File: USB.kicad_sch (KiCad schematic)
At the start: 4 parts, among them P1 USB_C_Plug, U7 FE1.1s

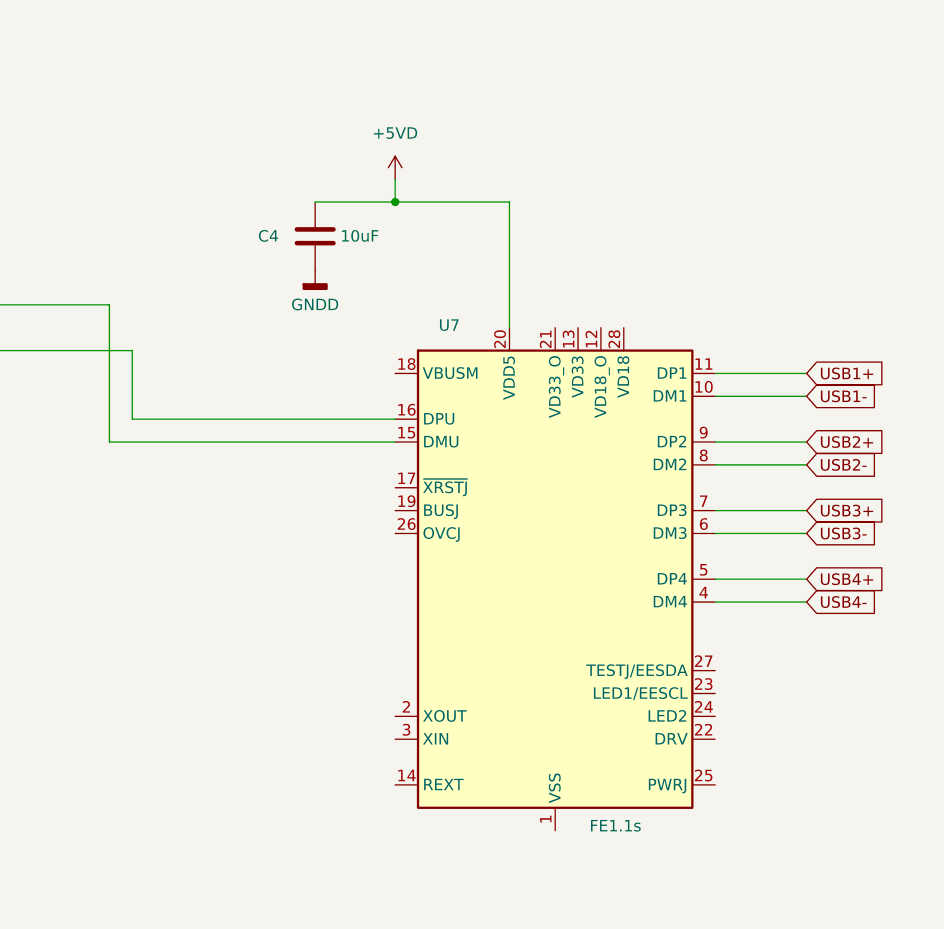
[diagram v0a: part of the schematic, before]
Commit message: Assign footprints to devices
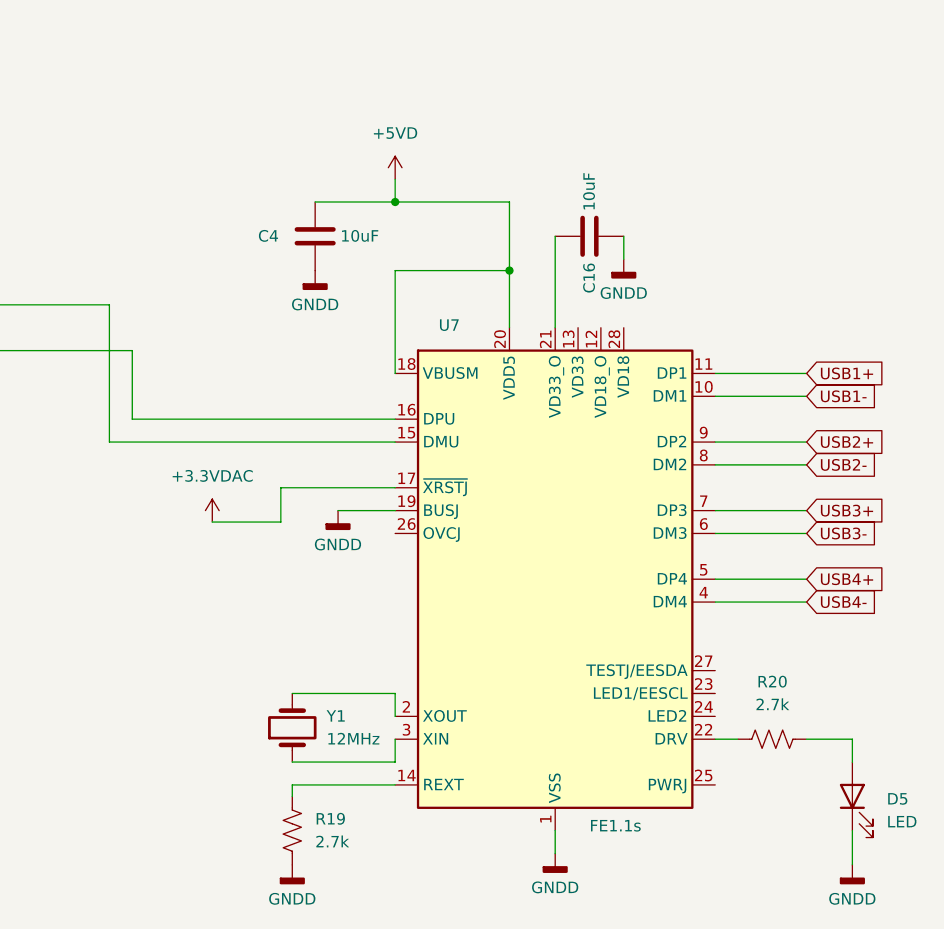
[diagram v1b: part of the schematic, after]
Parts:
- added C16: 10uF, Capacitor_SMD:C_0201_0603Metric, symbol Device:C
- added D5: LED, LED_SMD:LED_0201_0603Metric, symbol Device:LED
- added R19, R20: 2.7k, Resistor_SMD:R_0201_0603Metric, symbol Device:R_US
- added Y1: 12MHz, Crystal:Crystal_SMD_FOX_FE-2Pin_7.5x5.0mm_HandSoldering, symbol Device:Crystal
- C4: footprint (none) -> Capacitor_SMD:C_0201_0603Metric
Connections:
- net +5VD: now also U7.18 (VBUSM)
- net GNDD: now also U7.1 (VSS), U7.19 (BUSJ), C16.2, D5.1 (K), R19.2
- net at U7.14 (REXT): now also R19.1
- net +3.3VDAC: now reaches U7.17 (~{XRSTJ})
- net at U7.2 (XOUT): now also Y1.2
- net at U7.21 (VD33_O): now also C16.1
- net at U7.22 (DRV): now also R20.1
- net at U7.3 (XIN): now also Y1.1
- new net: D5.2 (A), R20.2

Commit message: Place Audio tranformers and cleanup routing.    Re-annotate based on geographical layout.
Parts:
- L1: footprint (none) -> Inductor_SMD:L_CommonModeChoke_Coilcraft_0805USB
- P1: footprint (none) -> Connector_USB:USB_C_Receptacle_GCT_USB4085
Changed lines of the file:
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@@
 			)
 		)
-		(property "Footprint" ""
+		(property "Footprint" "Inductor_SMD:L_CommonModeChoke_Coilcraft_0805USB"
 			(at 55.88 64.77 0)
 			(effects
@@
 			)
 		)
-		(property "Footprint" ""
+		(property "Footprint" "Connector_USB:USB_C_Receptacle_GCT_USB4085"
 			(at 44.45 99.06 0)
 			(effects

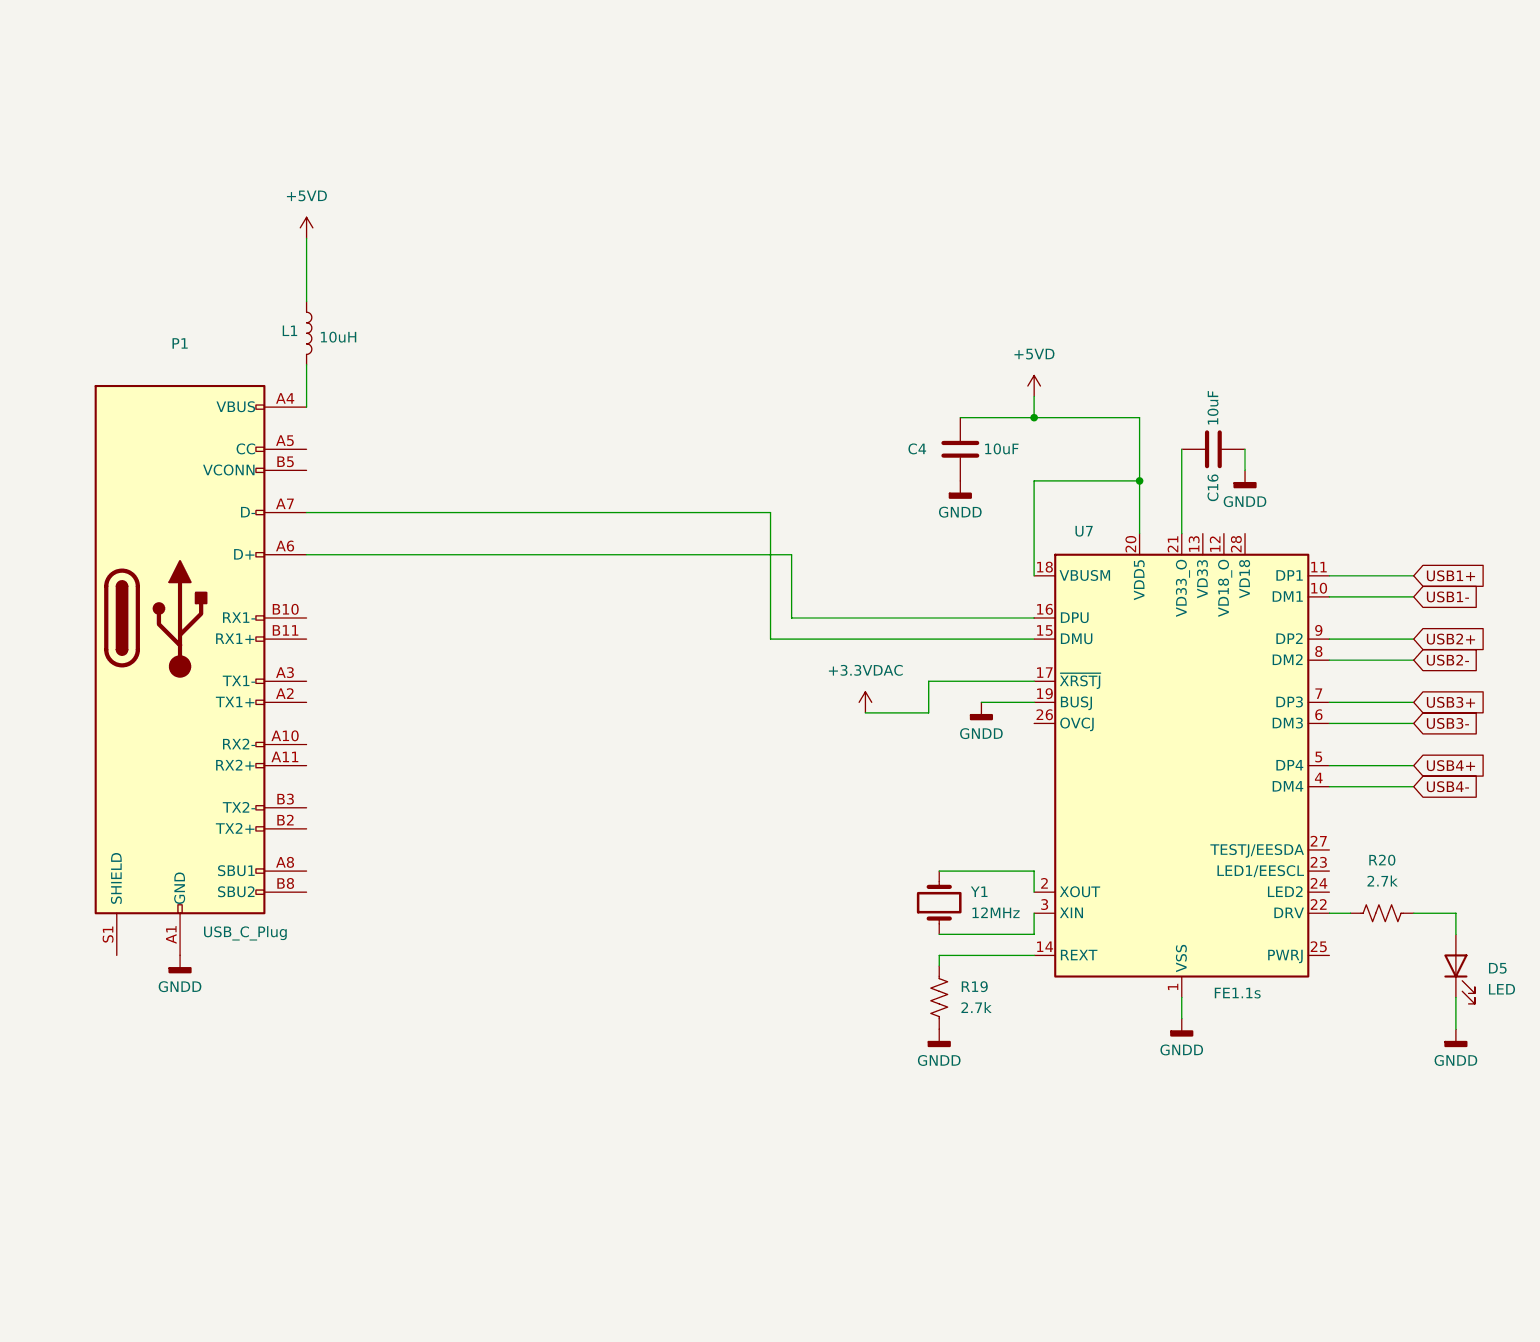
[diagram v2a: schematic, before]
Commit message: Move Radio interface onto it's own sheet, Add mounting holes and case outline
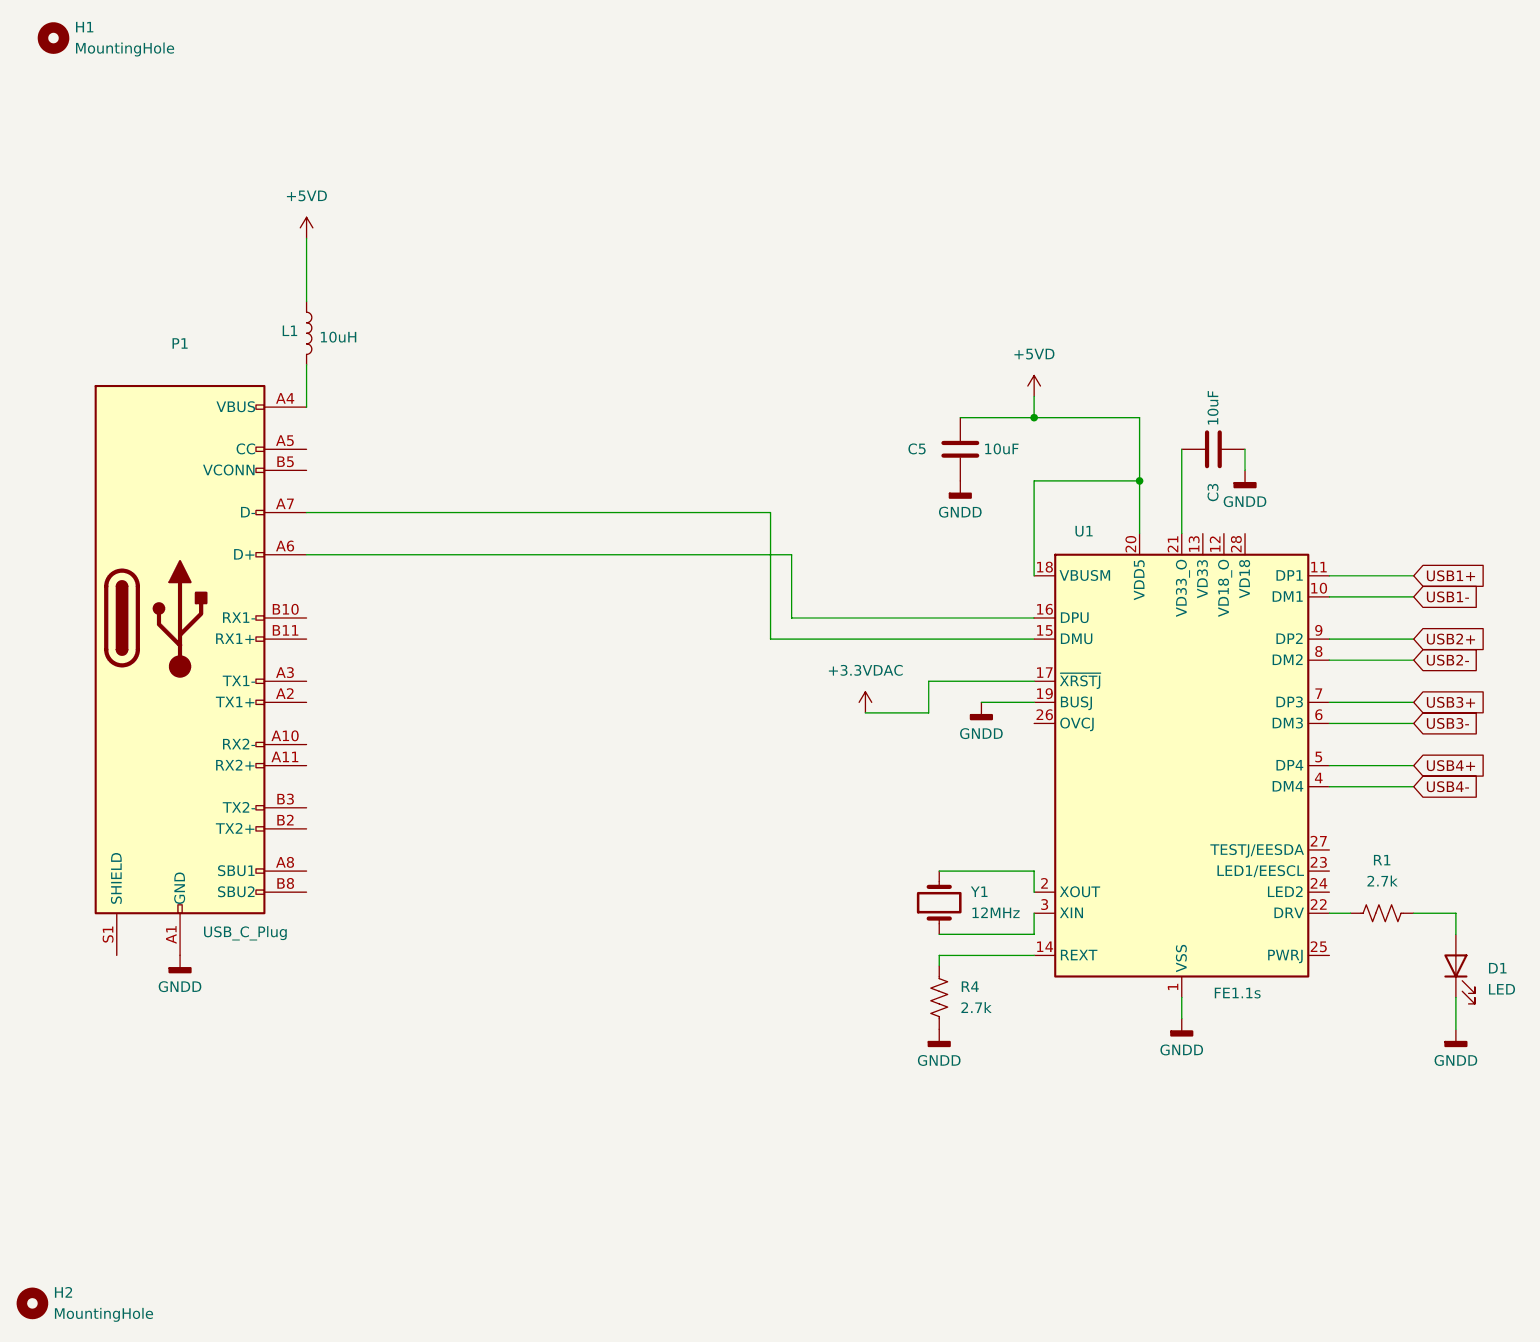
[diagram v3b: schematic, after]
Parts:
- added H1, H2: MountingHole, MountingHole:MountingHole_3.2mm_M3, symbol Mechanical:MountingHole
- renumbered C16 to C3, C4 to C5, D5 to D1, R20 to R1, R19 to R4, U7 to U1
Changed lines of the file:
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@@
 		(dnp no)
 		(fields_autoplaced yes)
-		(property "Reference" "D5"
+		(property "Reference" "D1"
 			(at 198.12 141.2874 90)
 			(effects
@@
 			(project "digital-mode-radio-interface"
 				(path "/a0d4bcf6-6cac-4e92-853e-9083f008b231/09c555a5-1bba-40e9-8ff5-2458ce056329"
-					(reference "D5")
+					(reference "D1")
+					(unit 1)
+				)
+			)
+		)
+	)
+	(symbol
+		(lib_id "Mechanical:MountingHole")
+		(at 22.86 181.61 0)
+		(unit 1)
+		(exclude_from_sim yes)
+		(in_bom no)
+		(on_board yes)
+		(dnp no)
+		(fields_autoplaced yes)
+		(property "Reference" "H2"
+			(at 25.4 180.3399 0)
+			(effects
+				(font
+					(size 1.27 1.27)
+				)
+				(justify left)
+			)
+		)
+		(property "Value" "MountingHole"
+			(at 25.4 182.8799 0)
+			(effects
+				(font
+					(size 1.27 1.27)
+				)
+				(justify left)
+			)
+		)
+		(property "Footprint" "MountingHole:MountingHole_3.2mm_M3"
+			(at 22.86 181.61 0)
+			(effects
+				(font
+					(size 1.27 1.27)
+				)
+				(hide yes)
+			)
+		)
+		(property "Datasheet" "~"
+			(at 22.86 181.61 0)
+			(effects
+				(font
+					(size 1.27 1.27)
+				)
+				(hide yes)
+			)
+		)
+		(property "Description" "Mounting Hole without connection"
+			(at 22.86 181.61 0)
+			(effects
+				(font
+					(size 1.27 1.27)
+				)
+				(hide yes)
+			)
+		)
+		(instances
+			(project "digital-mode-radio-interface"
+				(path "/a0d4bcf6-6cac-4e92-853e-9083f008b231/09c555a5-1bba-40e9-8ff5-2458ce056329"
+					(reference "H2")
 					(unit 1)
 				)
@@
 		(dnp no)
 		(fields_autoplaced yes)
-		(property "Reference" "R19"
+		(property "Reference" "R4"
 			(at 134.62 143.5099 0)
 			(effects
@@
 			(project "digital-mode-radio-interface"
 				(path "/a0d4bcf6-6cac-4e92-853e-9083f008b231/09c555a5-1bba-40e9-8ff5-2458ce056329"
-					(reference "R19")
+					(reference "R4")
 					(unit 1)
 				)
@@
 		(on_board yes)
 		(dnp no)
-		(property "Reference" "U7"
+		(property "Reference" "U1"
 			(at 148.336 88.646 0)
 			(effects
@@
 			(project "digital-mode-radio-interface"
 				(path "/a0d4bcf6-6cac-4e92-853e-9083f008b231/09c555a5-1bba-40e9-8ff5-2458ce056329"
-					(reference "U7")
+					(reference "U1")
 					(unit 1)
 				)
@@
 		(on_board yes)
 		(dnp no)
-		(property "Reference" "C4"
+		(property "Reference" "C5"
 			(at 128.27 78.74 0)
 			(effects
@@
 			(project "digital-mode-radio-interface"
 				(path "/a0d4bcf6-6cac-4e92-853e-9083f008b231/09c555a5-1bba-40e9-8ff5-2458ce056329"
-					(reference "C4")
+					(reference "C5")
 					(unit 1)
 				)
@@
 	)
 	(symbol
+		(lib_id "Mechanical:MountingHole")
+		(at 25.4 29.21 0)
+		(unit 1)
+		(exclude_from_sim yes)
+		(in_bom no)
+		(on_board yes)
+		(dnp no)
+		(fields_autoplaced yes)
+		(property "Reference" "H1"
+			(at 27.94 27.9399 0)
+			(effects
+				(font
+					(size 1.27 1.27)
+				)
+				(justify left)
+			)
+		)
+		(property "Value" "MountingHole"
+			(at 27.94 30.4799 0)
+			(effects
+				(font
+					(size 1.27 1.27)
+				)
+				(justify left)
+			)
+		)
+		(property "Footprint" "MountingHole:MountingHole_3.2mm_M3"
+			(at 25.4 29.21 0)
+			(effects
+				(font
+					(size 1.27 1.27)
+				)
+				(hide yes)
+			)
+		)
+		(property "Datasheet" "~"
+			(at 25.4 29.21 0)
+			(effects
+				(font
+					(size 1.27 1.27)
+				)
+				(hide yes)
+			)
+		)
+		(property "Description" "Mounting Hole without connection"
+			(at 25.4 29.21 0)
+			(effects
+				(font
+					(size 1.27 1.27)
+				)
+				(hide yes)
+			)
+		)
+		(instances
+			(project "digital-mode-radio-interface"
+				(path "/a0d4bcf6-6cac-4e92-853e-9083f008b231/09c555a5-1bba-40e9-8ff5-2458ce056329"
+					(reference "H1")
+					(unit 1)
+				)
+			)
+		)
+	)
+	(symbol
 		(lib_id "power:GNDD")
 		(at 132.08 148.59 0)
@@
 		(on_board yes)
 		(dnp no)
-		(property "Reference" "C16"
+		(property "Reference" "C3"
 			(at 165.1 85.09 0)
 			(effects
@@
 			(project "digital-mode-radio-interface"
 				(path "/a0d4bcf6-6cac-4e92-853e-9083f008b231/09c555a5-1bba-40e9-8ff5-2458ce056329"
-					(reference "C16")
+					(reference "C3")
 					(unit 1)
 				)
@@
 		(dnp no)
 		(fields_autoplaced yes)
-		(property "Reference" "R20"
+		(property "Reference" "R1"
 			(at 185.42 128.27 90)
 			(effects
@@
 			(project "digital-mode-radio-interface"
 				(path "/a0d4bcf6-6cac-4e92-853e-9083f008b231/09c555a5-1bba-40e9-8ff5-2458ce056329"
-					(reference "R20")
-					(unit 1)
-				)
+					(reference "R1")
+					(unit 1)
+				)

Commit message: kiCAD 9.0
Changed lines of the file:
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@@
 (kicad_sch
-	(version 20231120)
+	(version 20250114)
 	(generator "eeschema")
-	(generator_version "8.0")
+	(generator_version "9.0")
 	(paper "USLetter")
 	(title_block
